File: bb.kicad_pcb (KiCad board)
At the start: 2 copper layers, 162 x 153.9 mm, 49 parts, among them J2 AudioJack2, J4 USB_C_Receptacle_PowerOnly_6P, Q1 BC547/S9014, Q2 BC547/S9014, SW1 SW_DPST_x2, U1 ESP-12F, U2 LM1117MP-3.3

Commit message: updated to version 0.2
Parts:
- Battery1, Battery2: moved to B.Cu
- U1, U2: moved to F.Cu
- moved U1 28.9 mm to (107.5, 121.0)
- moved U2 4.05 mm to (112.3, 141.8), turned to -90 degrees
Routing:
- net A0: track 249.6 -> 292.6 mm
- net Net-(D10-A): track 73.0 -> 115.8 mm, vias 0 -> 1
- net Net-(D7-A): track 94.0 -> 134.1 mm, vias 0 -> 1
- net Net-(D6-A): track 92.6 -> 130.5 mm, vias 0 -> 1
- net Net-(D9-A): track 80.5 -> 115.4 mm, vias 0 -> 1
- net Net-(D8-A): track 85.9 -> 115.4 mm, vias 0 -> 1
- net Net-(D5-A): track 94.0 -> 122.5 mm, vias 0 -> 1
- net GND_ESP: track 435.8 -> 414.0 mm, vias 5 -> 3
- net Net-(U1-EN): track 48.9 -> 28.9 mm
- net Net-(U2-VI): track 40.7 -> 51.2 mm, vias 1 -> 0
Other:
- outline, holes or cut-outs redrawn
- board text added: "https://dennisdebel.nl"
- board text added: "l e d d i f f u s e r"
- board text added: "version 0.2"
- board text removed: "version 0.1"

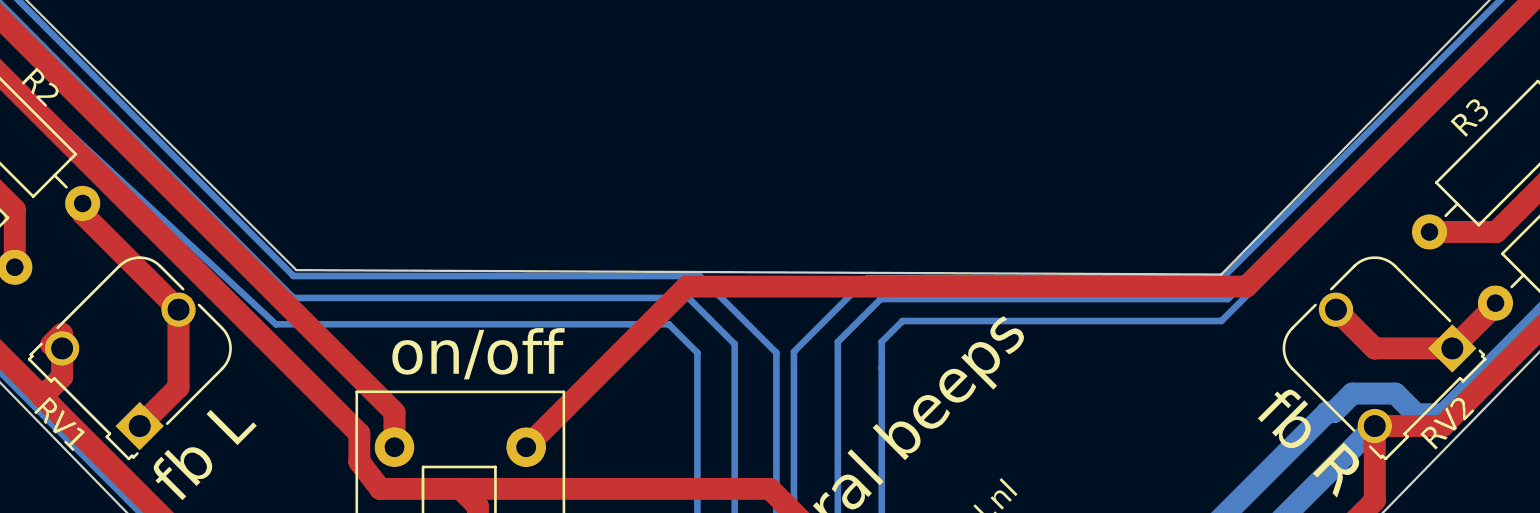
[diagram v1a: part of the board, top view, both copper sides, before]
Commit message: new gerbers (silk screen adjustment)
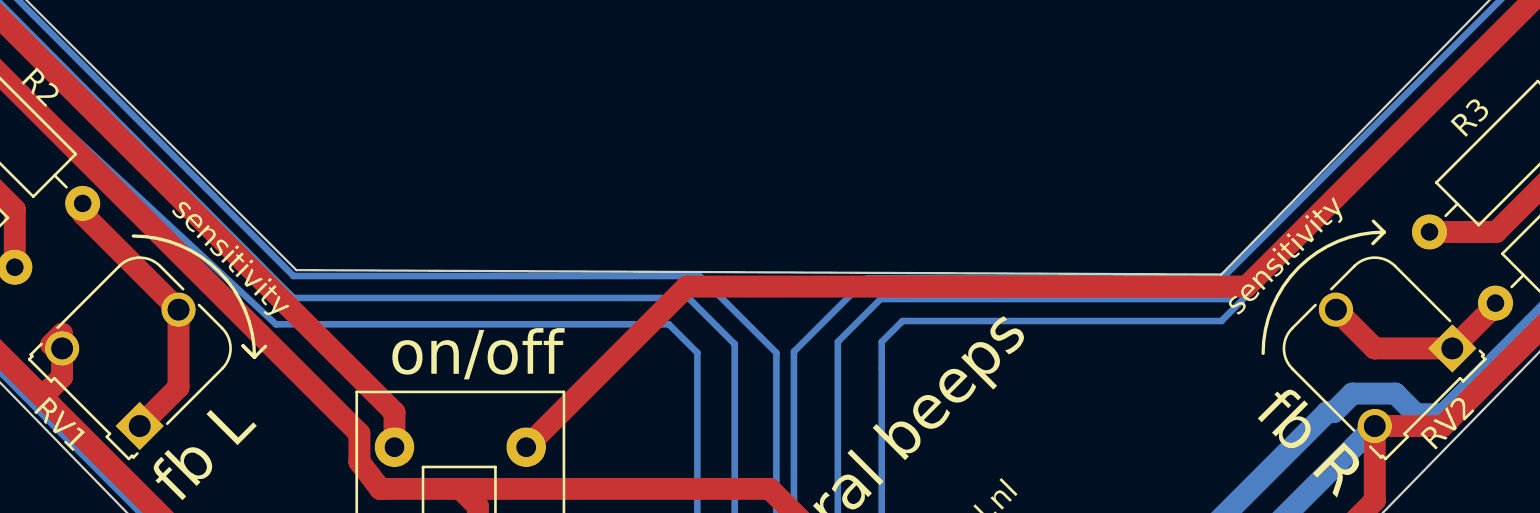
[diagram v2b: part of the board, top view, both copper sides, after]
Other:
- board text added: "sensitivity"
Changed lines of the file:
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@@
 		(layer "F.SilkS")
 	)
+	(gr_arc
+		(start 79 79.177321)
+		(mid 82.905124 80.794876)
+		(end 84.522679 84.7)
+		(stroke
+			(width 0.15)
+			(type default)
+		)
+		(layer "F.SilkS")
+	)
 	(gr_line
 		(start 113.892825 49.506477)
@@
 	)
 	(gr_line
+		(start 84 84.177321)
+		(end 84.522679 84.7)
+		(stroke
+			(width 0.15)
+			(type default)
+		)
+		(layer "F.SilkS")
+	)
+	(gr_line
 		(start 124.019434 49.205098)
 		(end 124.02375 49.208657)
@@
 	)
 	(gr_line
+		(start 136 79)
+		(end 135.5 78.5)
+		(stroke
+			(width 0.15)
+			(type default)
+		)
+		(layer "F.SilkS")
+	)
+	(gr_line
 		(start 109.507073 51.762397)
 		(end 109.515993 51.772186)
@@
 		(layer "F.SilkS")
 	)
+	(gr_arc
+		(start 130.477321 84.522679)
+		(mid 132.094876 80.617555)
+		(end 136 79)
+		(stroke
+			(width 0.15)
+			(type default)
+		)
+		(layer "F.SilkS")
+	)
 	(gr_line
 		(start 112.560621 49.705464)
@@
 	)
 	(gr_line
+		(start 84.522679 84.7)
+		(end 85.022679 84.2)
+		(stroke
+			(width 0.15)
+			(type default)
+		)
+		(layer "F.SilkS")
+	)
+	(gr_line
 		(start 124.298914 51.539142)
 		(end 124.307494 51.446806)
@@
 	)
 	(gr_line
+		(start 84.522679 84.7)
+		(end 84 84.177321)
+		(stroke
+			(width 0.15)
+			(type default)
+		)
+		(layer "F.SilkS")
+	)
+	(gr_line
 		(start 116.539683 51.781494)
 		(end 116.548297 51.763512)
@@
 	)
 	(gr_line
+		(start 136 79)
+		(end 135.477321 79.522679)
+		(stroke
+			(width 0.15)
+			(type default)
+		)
+		(layer "F.SilkS")
+	)
+	(gr_line
 		(start 110.823008 49.436779)
 		(end 110.831839 49.459668)
@@
 		)
 	)
+	(gr_text "sensitivity"
+		(at 80.6 78.1 -45)
+		(layer "F.SilkS")
+		(effects
+			(font
+				(size 1 1)
+				(thickness 0.15)
+			)
+			(justify left bottom)
+		)
+	)
 	(gr_text "binaural beeps"
 		(at 105.6 98.3 45)
@@
 		)
 	)
+	(gr_text "sensitivity"
+		(at 129.4 82.922679 45)
+		(layer "F.SilkS")
+		(effects
+			(font
+				(size 1 1)
+				(thickness 0.15)
+			)
+			(justify left bottom)
+		)
+	)

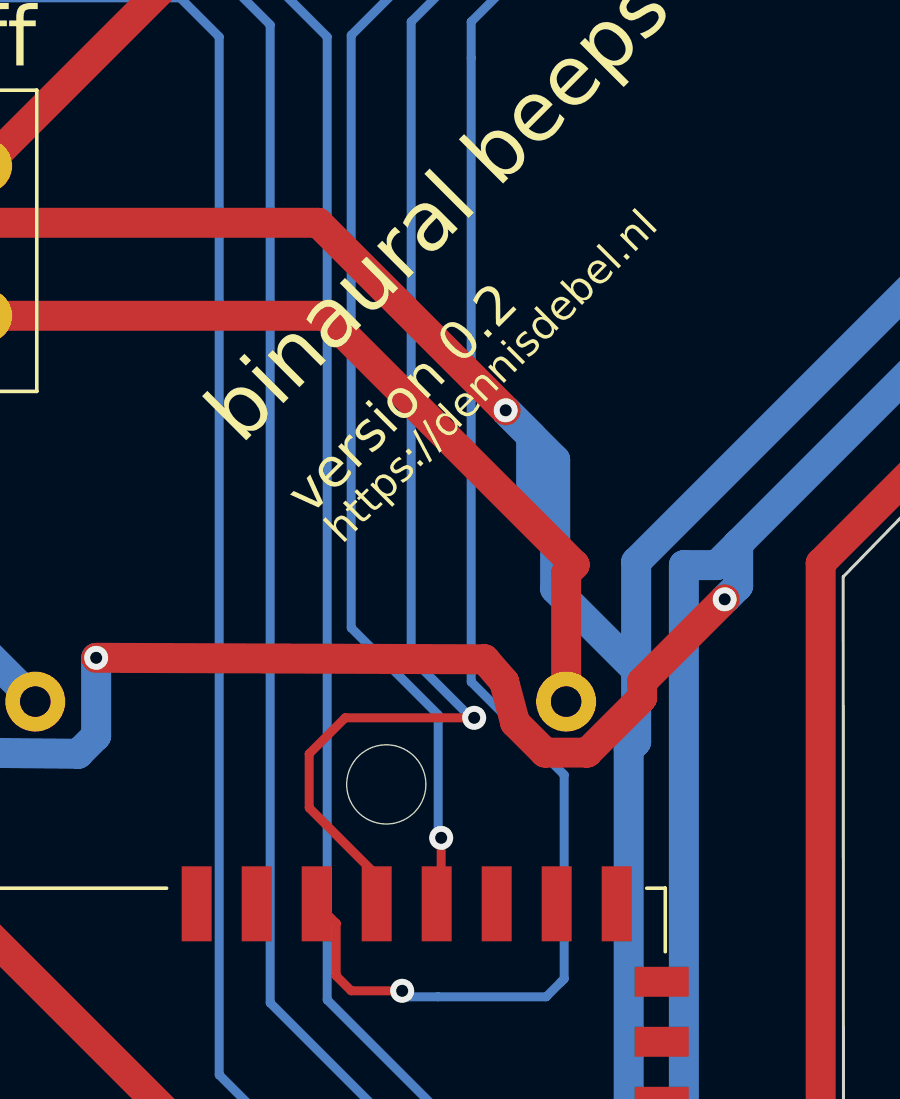
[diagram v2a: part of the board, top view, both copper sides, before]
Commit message: Version 0.3
ESP ground bodge fix
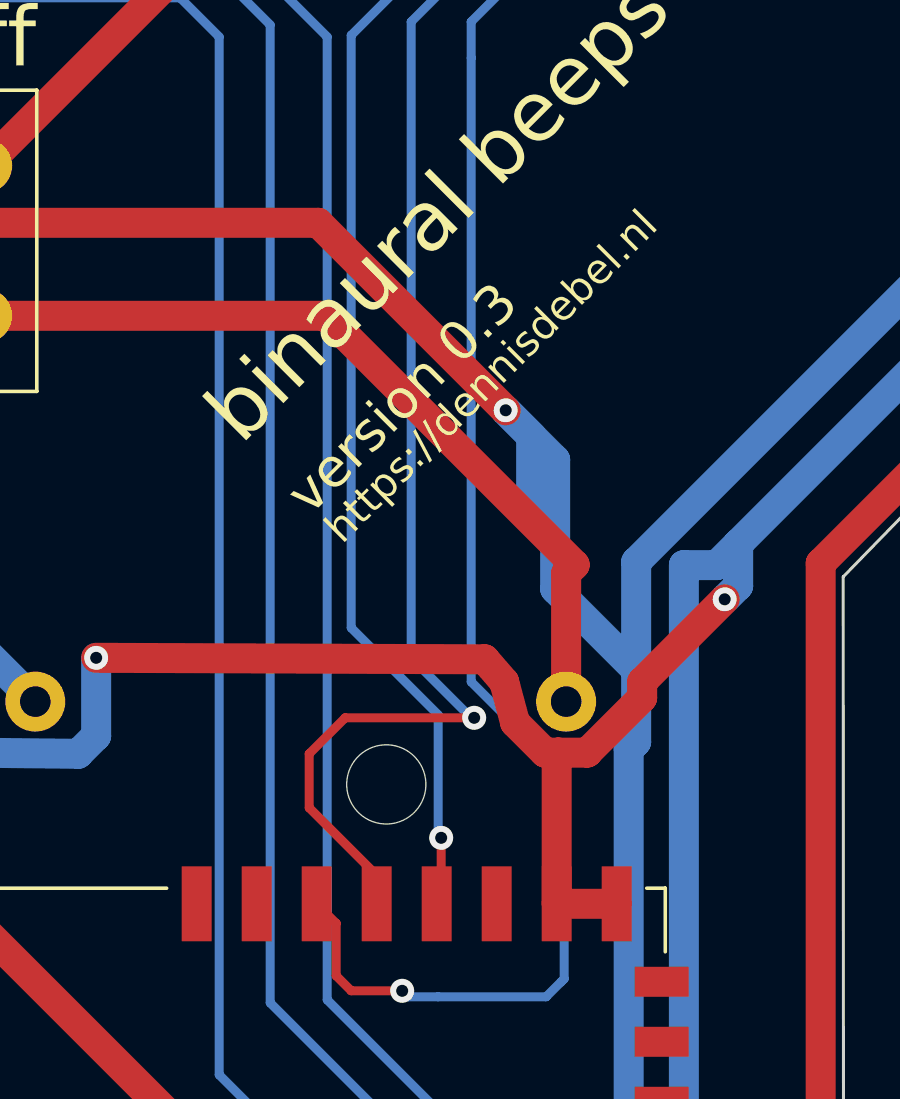
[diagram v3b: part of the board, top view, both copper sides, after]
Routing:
- net GND_ESP: track 414.0 -> 421.1 mm
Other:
- board text added: "version 0.3"
- board text removed: "version 0.2"
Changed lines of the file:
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@@
 		(fp_arc
 			(start 0.215816 -1.115611)
-			(mid 0.446097 -1.502143)
+			(mid 0.446099 -1.502142)
 			(end 0.74 -1.842816)
 			(stroke
@@
 		(fp_arc
 			(start 4.34 -1.842819)
-			(mid 4.633905 -1.502147)
+			(mid 4.633904 -1.502147)
 			(end 4.864184 -1.115612)
 			(stroke
@@
 		(fp_arc
 			(start 2.54 2.607183)
-			(mid 1.143021 2.2)
+			(mid 1.14302 2.200002)
 			(end 0.183599 1.10599)
 			(stroke
@@
 		(fp_arc
 			(start 4.896401 1.10599)
-			(mid 3.936979 2.199999)
+			(mid 3.936978 2.2)
 			(end 2.54 2.607183)
 			(stroke
@@
 		)
 		(fp_text user "${REFERENCE}"
-			(at 0 0 360)
+			(at 0 0 0)
 			(layer "F.Fab")
 			(effects
@@
 		(fp_arc
 			(start 0.215816 -1.215611)
-			(mid 0.446099 -1.602142)
+			(mid 0.4461 -1.602142)
 			(end 0.74 -1.942817)
 			(stroke
@@
 		(fp_arc
 			(start 4.34 -1.942818)
-			(mid 4.633905 -1.602146)
+			(mid 4.633904 -1.602146)
 			(end 4.864184 -1.215612)
 			(stroke
@@
 		(tags "AA battery cell holder")
 		(property "Reference" "Battery2"
-			(at 28.6 -0.005 360)
+			(at 28.6 -0.005 0)
 			(layer "B.SilkS")
 			(effects
@@
 		(tags "AA battery cell holder")
 		(property "Reference" "Battery1"
-			(at 28.6 0 360)
+			(at 28.6 0 0)
 			(layer "B.SilkS")
 			(effects
@@
 		)
 	)
-	(gr_text "version 0.2"
+	(gr_text "version 0.3"
 		(at 107.827387 100.598097 45)
 		(layer "F.SilkS")
@@
 			(justify left bottom)
 		)
-		(render_cache "version 0.2" 45
+		(render_cache "version 0.3" 45
 			(polygon
 				(pts
@@
 			(polygon
 				(pts
-					(xy 113.100398 94.788924) (xy 112.993752 94.041954) (xy 112.98014 93.976152) (xy 112.960973 93.922511)
-					(xy 112.928883 93.864552) (xy 112.902823 93.833378) (xy 112.9017 93.832255) (xy 112.848454 93.793217)
-					(xy 112.784053 93.779269) (xy 112.722367 93.79549) (xy 112.669589 93.83335) (xy 112.66214 93.840562)
-					(xy 112.62347 93.891953) (xy 112.604849 93.956263) (xy 112.604439 93.96472) (xy 112.614953 94.028224)
-					(xy 112.646398 94.087762) (xy 112.655854 94.100553) (xy 112.656527 94.101227) (xy 112.523164 94.23459)
-					(xy 112.52249 94.233917) (xy 112.484932 94.177441) (xy 112.454102 94.115166) (xy 112.434255 94.052731)
-					(xy 112.425193 93.985387) (xy 112.429329 93.919747) (xy 112.439419 93.876934) (xy 112.465656 93.814851)
-					(xy 112.501189 93.760993) (xy 112.538431 93.719098) (xy 112.590087 93.672967) (xy 112.642621 93.637009)
-					(xy 112.701421 93.609206) (xy 112.706819 93.607289) (xy 112.771164 93.592239) (xy 112.834878 93.592218)
-					(xy 112.877003 93.600553) (xy 112.938812 93.625422) (xy 112.993418 93.661143) (xy 113.036635 93.699565)
-					(xy 113.037309 93.700239) (xy 113.079481 93.751291) (xy 113.112522 93.808643) (xy 113.118809 93.822152)
-					(xy 113.142218 93.883659) (xy 113.159181 93.949242) (xy 113.164835 93.980886) (xy 113.26003 94.607739)
-					(xy 113.607359 94.26041) (xy 113.729945 94.382996) (xy 113.212208 94.900734)
+					(xy 113.472873 94.658929) (xy 113.423777 94.702543) (xy 113.367543 94.740085) (xy 113.308975 94.766697)
+					(xy 113.243661 94.782841) (xy 113.177716 94.785472) (xy 113.133402 94.779719) (xy 113.067184 94.75966)
+					(xy 113.007593 94.729401) (xy 112.959626 94.696198) (xy 113.090968 94.564856) (xy 113.146642 94.596148)
+					(xy 113.179877 94.60482) (xy 113.245086 94.600652) (xy 113.266317 94.593369) (xy 113.321141 94.560324)
+					(xy 113.349164 94.535219) (xy 113.390633 94.482486) (xy 113.41279 94.419337) (xy 113.414049 94.40208)
+					(xy 113.40145 94.338557) (xy 113.364676 94.282383) (xy 113.353654 94.270738) (xy 113.325814 94.242898)
+					(xy 113.273834 94.200327) (xy 113.212474 94.173726) (xy 113.185939 94.169929) (xy 113.121597 94.180447)
+					(xy 113.06546 94.216079) (xy 113.053923 94.226957) (xy 112.988813 94.292067) (xy 112.866226 94.16948)
+					(xy 112.931337 94.10437) (xy 112.969309 94.052288) (xy 112.982527 93.988968) (xy 112.963823 93.924016)
+					(xy 112.92463 93.871857) (xy 112.921009 93.868178) (xy 112.89272 93.839889) (xy 112.840351 93.801235)
+					(xy 112.777542 93.787127) (xy 112.713846 93.804575) (xy 112.662817 93.842637) (xy 112.659221 93.846175)
+					(xy 112.620703 93.898586) (xy 112.612746 93.917347) (xy 112.604423 93.982859) (xy 112.60646 93.999072)
+					(xy 112.62778 94.060447) (xy 112.644628 94.089328) (xy 112.513958 94.219997) (xy 112.479106 94.165043)
+					(xy 112.450695 94.10439) (xy 112.432683 94.043526) (xy 112.424958 93.978023) (xy 112.429736 93.914541)
+					(xy 112.439868 93.873342) (xy 112.465389 93.81389) (xy 112.503224 93.757785) (xy 112.535288 93.722241)
+					(xy 112.587592 93.675932) (xy 112.640777 93.640732) (xy 112.702638 93.614106) (xy 112.765651 93.601989)
+					(xy 112.781583 93.601227) (xy 112.852233 93.608928) (xy 112.913214 93.63125) (xy 112.972484 93.668138)
+					(xy 113.02294 93.712363) (xy 113.037982 93.727405) (xy 113.07887 93.777101) (xy 113.108648 93.836579)
+					(xy 113.120829 93.884792) (xy 113.12286 93.951442) (xy 113.108411 94.01904) (xy 113.089621 94.064631)
+					(xy 113.147575 94.035189) (xy 113.212945 94.01972) (xy 113.280012 94.021972) (xy 113.346788 94.041708)
+					(xy 113.405513 94.074614) (xy 113.456754 94.116414) (xy 113.467933 94.127271) (xy 113.482976 94.142314)
+					(xy 113.527884 94.193273) (xy 113.564975 94.251) (xy 113.589173 94.310477) (xy 113.600907 94.376307)
+					(xy 113.597045 94.442452) (xy 113.585805 94.486724) (xy 113.559191 94.547084) (xy 113.523899 94.600898)
+					(xy 113.47804 94.653703)
 				)
 			)
@@
 	)
 	(segment
+		(start 115.95 113.4)
+		(end 115.95 108.41)
+		(width 1)
+		(layer "F.Cu")
+		(net 5)
+	)
+	(segment
 		(start 139.578979 54.602452)
 		(end 136.786657 54.602452)
@@
 	)
 	(segment
+		(start 115.561061 108.36)
+		(end 116 108.36)
+		(width 1)
+		(layer "F.Cu")
+		(net 5)
+	)
+	(segment
 		(start 124.75 150.6)
 		(end 124.95 150.8)
@@
 	)
 	(segment
-		(start 115.561061 108.36)
-		(end 116.969389 108.36)
+		(start 121.650225 169.05)
+		(end 119.520225 171.18)
 		(width 1)
 		(layer "F.Cu")
@@
 	)
 	(segment
-		(start 121.650225 169.05)
-		(end 119.520225 171.18)
+		(start 117.95 113.4)
+		(end 115.95 113.4)
 		(width 1)
 		(layer "F.Cu")
@@
 	)
 	(segment
+		(start 116 108.36)
+		(end 116.969389 108.36)
+		(width 1)
+		(layer "F.Cu")
+		(net 5)
+	)
+	(segment
 		(start 78.329137 54.602452)
 		(end 79.415794 53.515795)
@@
 		(width 1)
 		(layer "F.Cu")
+		(net 5)
+	)
+	(segment
+		(start 115.95 108.41)
+		(end 116 108.36)
+		(width 1)
+		(layer "F.Cu")

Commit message: added annotion ground issue
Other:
- board text added: "the gnd of esp is missing in verion 0.2"
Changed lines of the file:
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@@
 		(layer "Edge.Cuts")
+	)
+	(gr_circle
+		(center 117.066905 112.9)
+		(end 121.73381 112.9)
+		(stroke
+			(width 1)
+			(type default)
+		)
+		(fill none)
+		(layer "User.3")
 	)
 	(gr_text "l  e  d   d  i  f  f  u  s  e  r "
@@
 		)
 	)
+	(gr_text "the gnd of esp is missing in verion 0.2"
+		(at 127.2 113.8 0)
+		(layer "User.3")
+		(effects
+			(font
+				(size 1 1)
+				(thickness 0.15)
+			)
+			(justify left bottom)
+		)
+	)

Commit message: typo
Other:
- board text added: "the gnd of esp is missing in version 0.2"
- board text removed: "the gnd of esp is missing in verion 0.2"
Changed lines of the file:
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@@
 		)
 	)
-	(gr_text "the gnd of esp is missing in verion 0.2"
+	(gr_text "the gnd of esp is missing in version 0.2"
 		(at 127.2 113.8 0)
 		(layer "User.3")
